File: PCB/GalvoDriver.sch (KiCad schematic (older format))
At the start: 30 parts, among them J1 Screw_Terminal_01x03, J2 Conn_01x03, J3 Conn_01x05_Male, J4 JUMPER_A, J5 JUMPER_B, J6 AudioJack3, J7 Conn_01x03, J8 Screw_Terminal_01x04, Q1 PN2222A, U1 TL082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

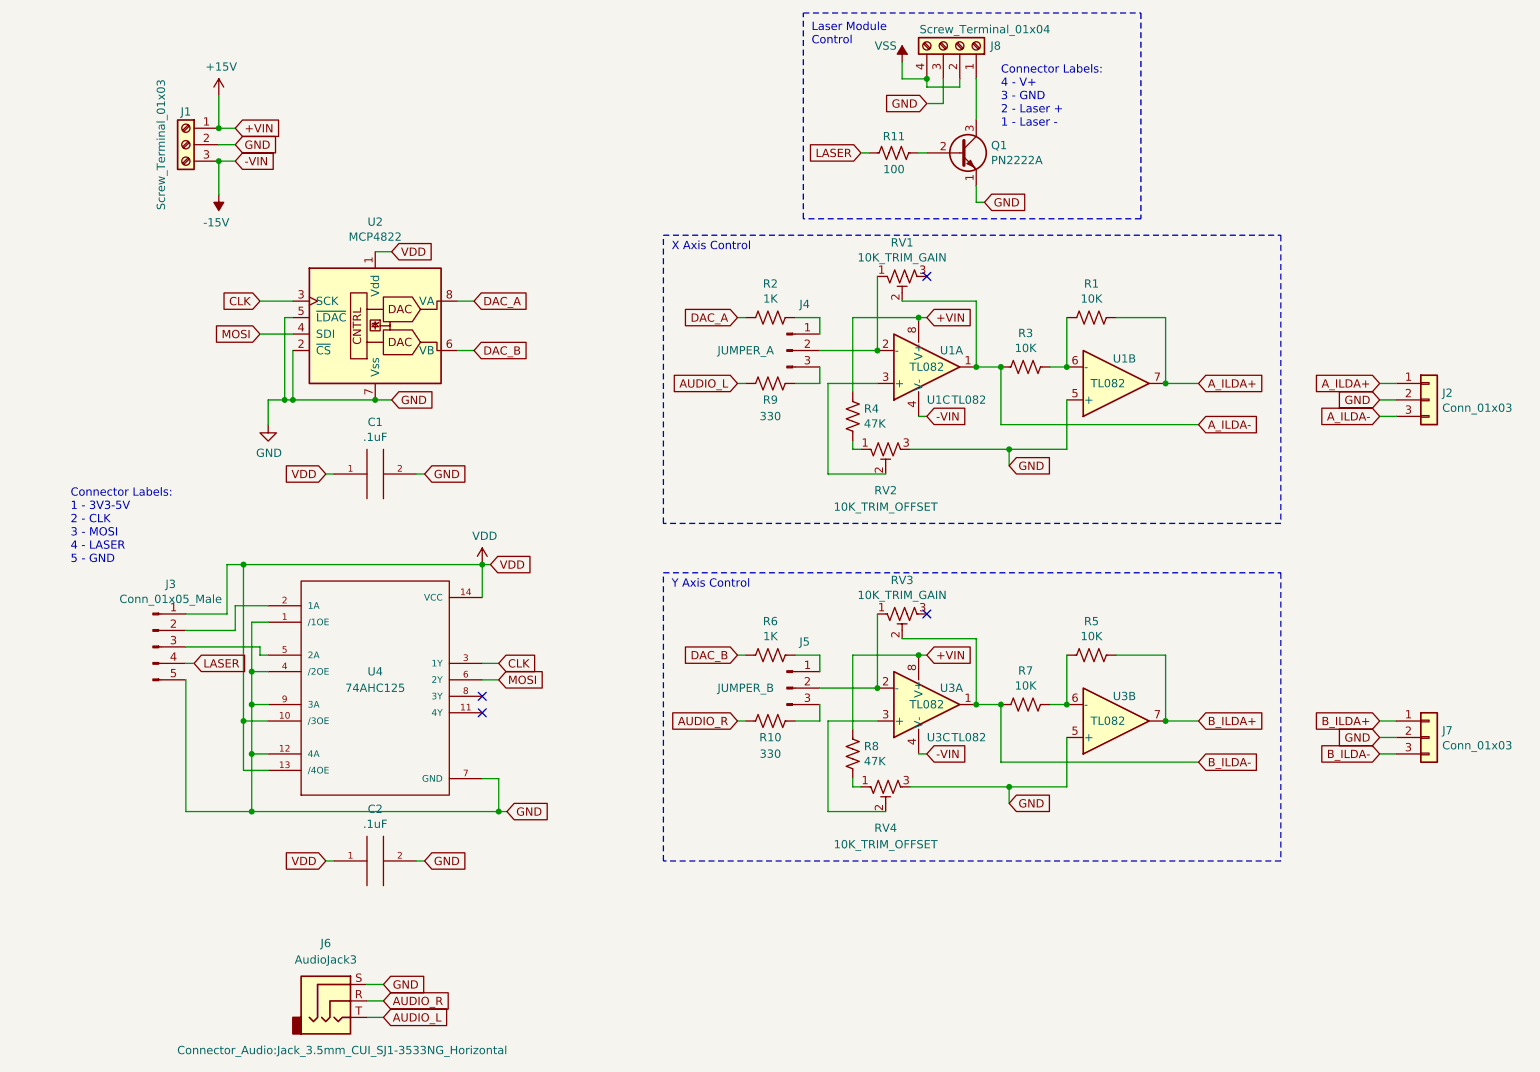
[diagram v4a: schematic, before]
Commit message: Added CS connection to header, buffer, DAC input
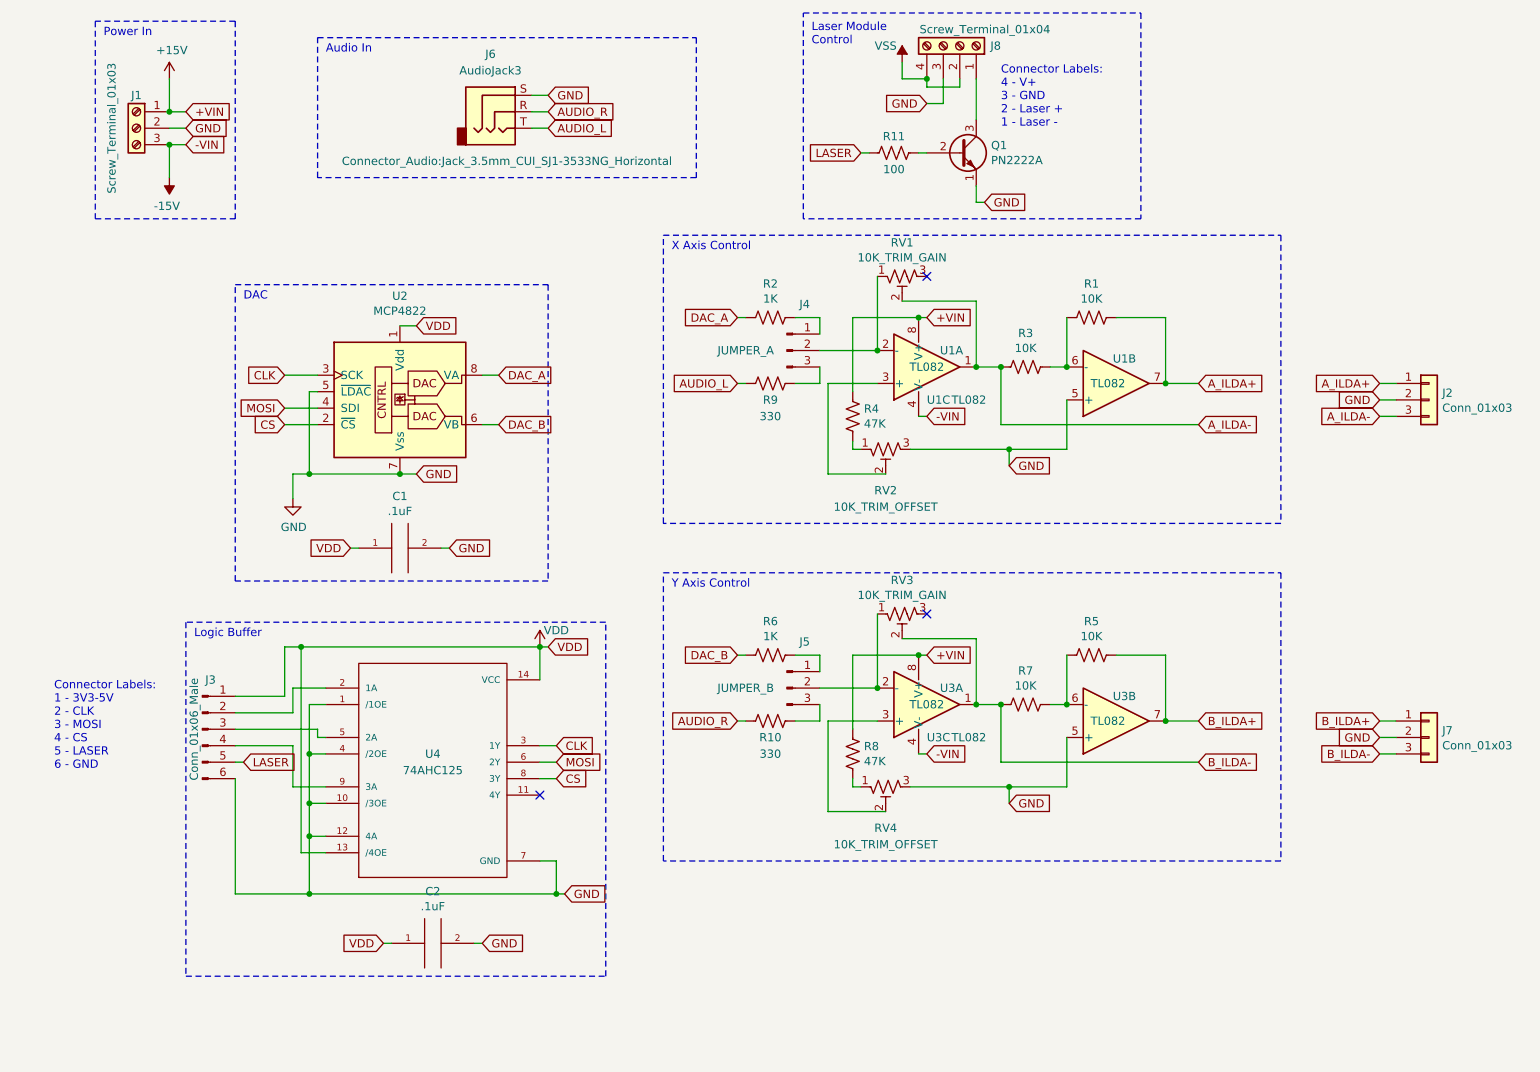
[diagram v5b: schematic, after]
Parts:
- removed J3: Conn_01x05_Male, Pin_Headers:Pin_Header_Straight_1x05_Pitch2.54mm, symbol Connector:Conn_01x05_Male
- added J3: Conn_01x06_Male, Pin_Headers:Pin_Header_Straight_1x06_Pitch2.54mm, symbol Connector:Conn_01x06_Male
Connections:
- net GND: now also U4.10 (/3OE), J3.6 (Pin_6); no longer U2.2 (~CS), U4.9 (3A)
- net LASER: now also J3.5 (Pin_5)
- net VDD: now also J3.1 (Pin_1); no longer U4.10 (/3OE)
- net at U4.2 (1A): now also J3.2 (Pin_2)
- net at U4.5 (2A): now also J3.3 (Pin_3)
- net CS: now reaches U4.8 (3Y)
- net CS: now also U2.2 (~CS)
- new net: J3.4 (Pin_4), U4.9 (3A)
- no-connect marks 4 -> 3
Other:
- note added: "Audio In"
- note added: "Connector Labels:\n1 - 3V3-5V\n2 - CLK\n3 - MOSI\n4 - CS\n5 - LASER\n6 - GND"
- note added: "DAC"
- note added: "Logic Buffer"
- note added: "Power In"
- note removed: "Connector Labels:\n1 - 3V3-5V\n2 - CLK\n3 - MOSI\n4 - LASER\n5 - GND"
- moved on the sheet: C1, C2, J1, J6, U2, U4

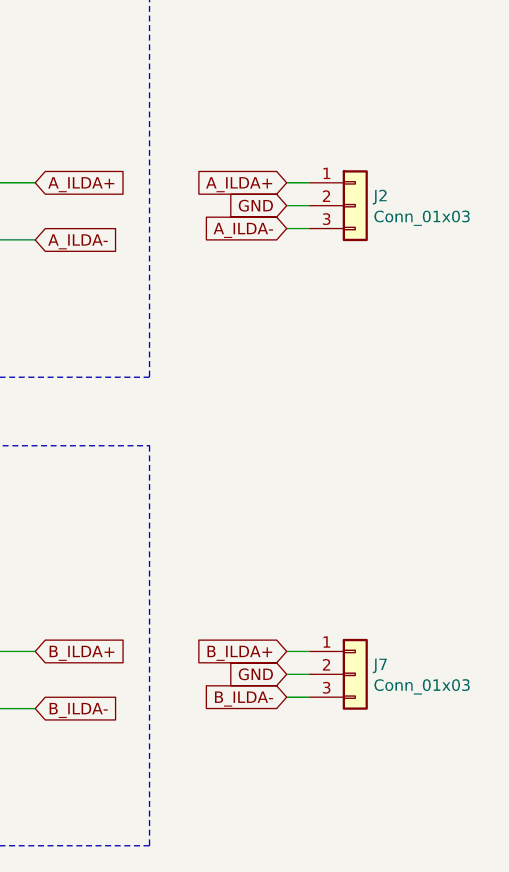
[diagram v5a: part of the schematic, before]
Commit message: Flipped ILDA connector wiring and silkscreen labels
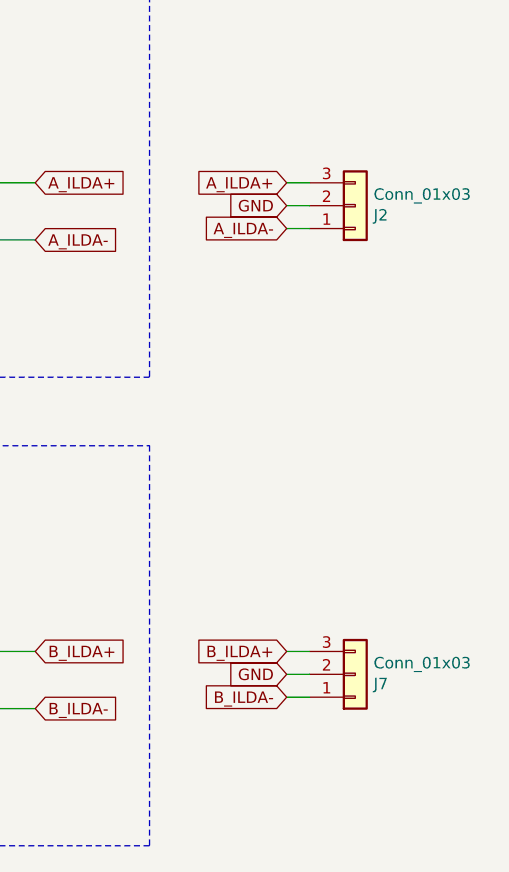
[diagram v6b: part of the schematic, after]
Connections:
- net A_ILDA+: now also J2.3 (Pin_3); no longer J2.1 (Pin_1)
- net A_ILDA-: now also J2.1 (Pin_1); no longer J2.3 (Pin_3)
- net B_ILDA+: now also J7.3 (Pin_3); no longer J7.1 (Pin_1)
- net B_ILDA-: now also J7.1 (Pin_1); no longer J7.3 (Pin_3)
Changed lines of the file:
@@
 F 4 "https://www.digikey.com/product-detail/en/jst-sales-america-inc/XHP-3/455-2219-ND/1651017" H 8950 2900 50  0001 C CNN "DigiKey"
 	1    8950 2900
-	1    0    0    -1
+	1    0    0    1
 $EndComp
 $Comp
@@
 F 4 "https://www.digikey.com/product-detail/en/jst-sales-america-inc/XHP-3/455-2219-ND/1651017" H 8950 4950 50  0001 C CNN "DigiKey"
 	1    8950 4950
-	1    0    0    -1
+	1    0    0    1
 $EndComp
 Wire Wire Line
